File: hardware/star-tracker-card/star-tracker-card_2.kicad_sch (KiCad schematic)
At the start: 93 parts, among them Q2 DMN3028LQ-7, Q3 DMP2240UDM, Q4 DMN3028LQ-7, Q5 DMP3050LVT-7, Q6 DMP3050LVT-7, U12 MIC842LYC5, U13 MIC842LYC5, U14 MAX4211FETE, U15 TPS62112, U16 MAX7310ATE, U2 TS5A21366DCUR

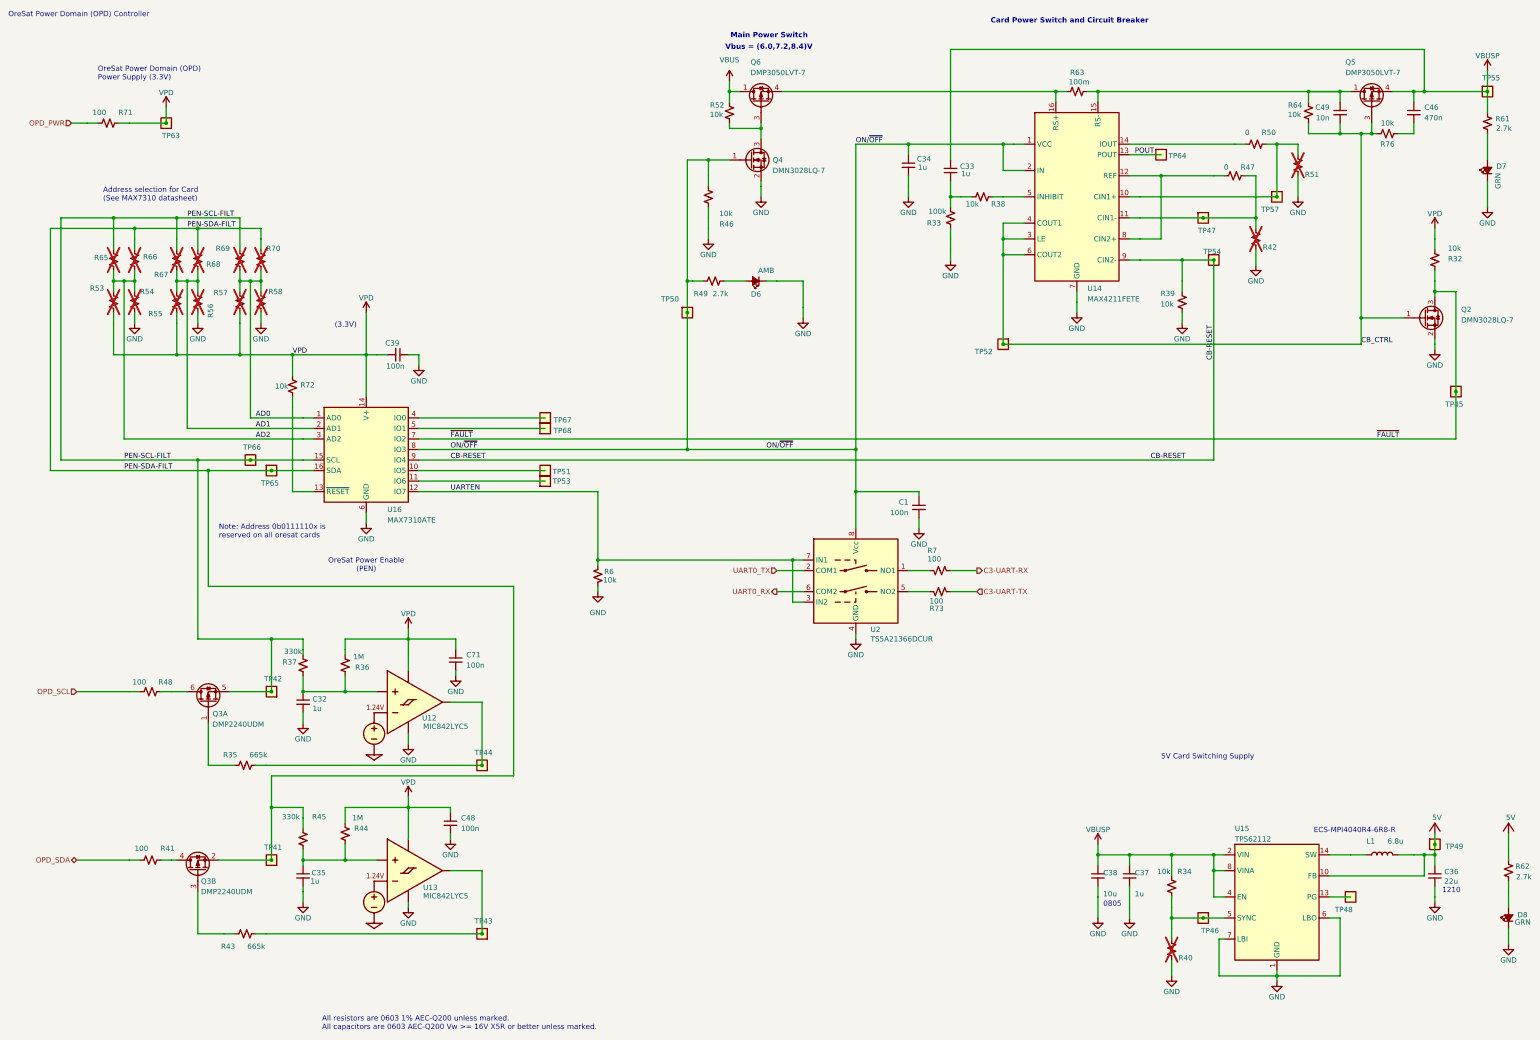
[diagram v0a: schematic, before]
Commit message: Star Tracker v1.3 files, including new Makefile, Readme, and fixes in ERC, DRC, and layout
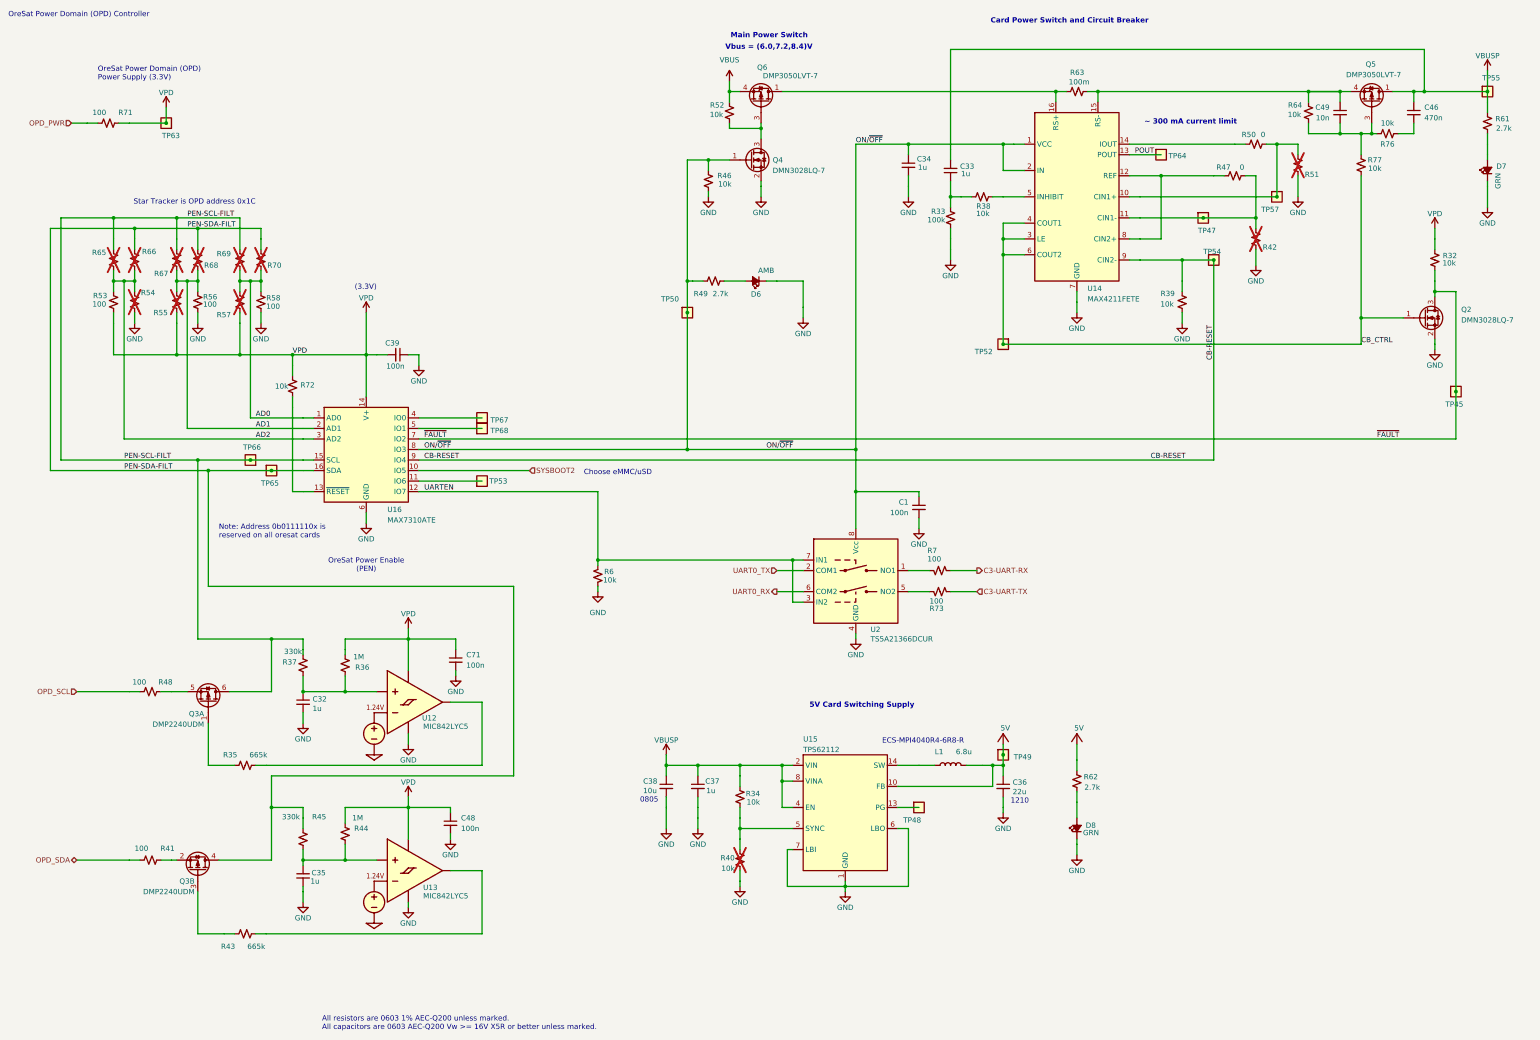
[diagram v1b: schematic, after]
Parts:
- removed TP41, TP42, TP43, TP44, TP46, TP51: TEST-POINT, star-tracker-card:2MM-TEST-POINT, symbol star-tracker-card-eagle-import:TEST-POINT
- added R77: 10k, oresat-passives:0603-C-NOSILK, symbol Device:R_Small_US
- Q2, Q4: footprint star-tracker-card:SOT23 -> Package_TO_SOT_SMD:SOT-23-3
- Q3: footprint star-tracker-card:SOT23-6 -> Package_TO_SOT_SMD:TSOT-23-6
- R35, R42, R43, R51: footprint Resistor_SMD:R_0603_1608Metric -> oresat-passives:0603-C-NOSILK
- R40: value NP -> 10k; footprint Resistor_SMD:R_0603_1608Metric -> oresat-passives:0603-C-NOSILK
- R53, R56, R58: value NP -> 100; footprint Resistor_SMD:R_0603_1608Metric -> oresat-passives:0603-C-NOSILK; DIS Digi-Key -> DigiKey; DPN 1276-4275-1-ND -> RMCF0603FT100RCT-ND; MFR Samsung -> Stackpole Electronics; MPN RC1005F6653CS -> RMCF0603FT100R; now fitted
- R54, R55, R57, R65, R66, R67, R68, R69, R70: value NP -> 100; footprint Resistor_SMD:R_0603_1608Metric -> oresat-passives:0603-C-NOSILK
- TP45, TP47, TP48, TP49, TP50, TP52, TP53, TP54, TP55, TP57, TP63, TP64, TP65, TP66, TP67, TP68: now left out of the parts list
- U16: DIS (none) -> DigiKey; DPN (none) -> 175-MAX7310ATE+TCT-ND; MFR Maxim -> Analog Devices Inc./Maxim Integrated; MPN MAX7310ATE -> MAX7310ATE+T
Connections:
- net CB_CTRL: now also R77.2; no longer C49.2, Q5.3 (G), R64.1, R76.2
- net PEN-SCL-FILT: now also Q3.6 (D); no longer Q3.5 (S)
- net PEN-SDA-FILT: now also Q3.4 (D); no longer Q3.2 (S)
- net VBUS: now also Q6.4 (S); no longer Q6.1 (D), Q6.2 (D), Q6.5 (D), Q6.6 (D)
- net VBUSP: now also Q5.1 (D), Q5.2 (D), Q5.5 (D), Q5.6 (D); no longer Q5.4 (S)
- net at R41.2: now also Q3.2 (S); no longer Q3.4 (D)
- net SYSBOOT2: now reaches U16.10 (IO5)
- net at R63.1, U14.16 (RS+): now also Q6.1 (D), Q6.2 (D), Q6.5 (D), Q6.6 (D); no longer Q6.4 (S)
- net at C49.1, R63.2, R64.2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: now also Q5.4 (S); no longer Q5.1 (D), Q5.2 (D), Q5.5 (D), Q5.6 (D)
- net at R48.2: now also Q3.5 (S); no longer Q3.6 (D)
- new net: C49.2, Q5.3 (G), R64.1, R76.2, R77.1
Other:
- note added: "Choose eMMC/uSD"
- note added: "Star Tracker is OPD address 0x1C"
- note added: "~ 300 mA current limit"
- note removed: "Address selection for Card (See MAX7310 datasheet)"
- moved on the sheet: C36, C37, C38, D8, L1, Q3A, Q3B, Q5, Q6, R34, R40, R46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
